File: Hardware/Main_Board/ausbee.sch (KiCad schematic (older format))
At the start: 0 parts

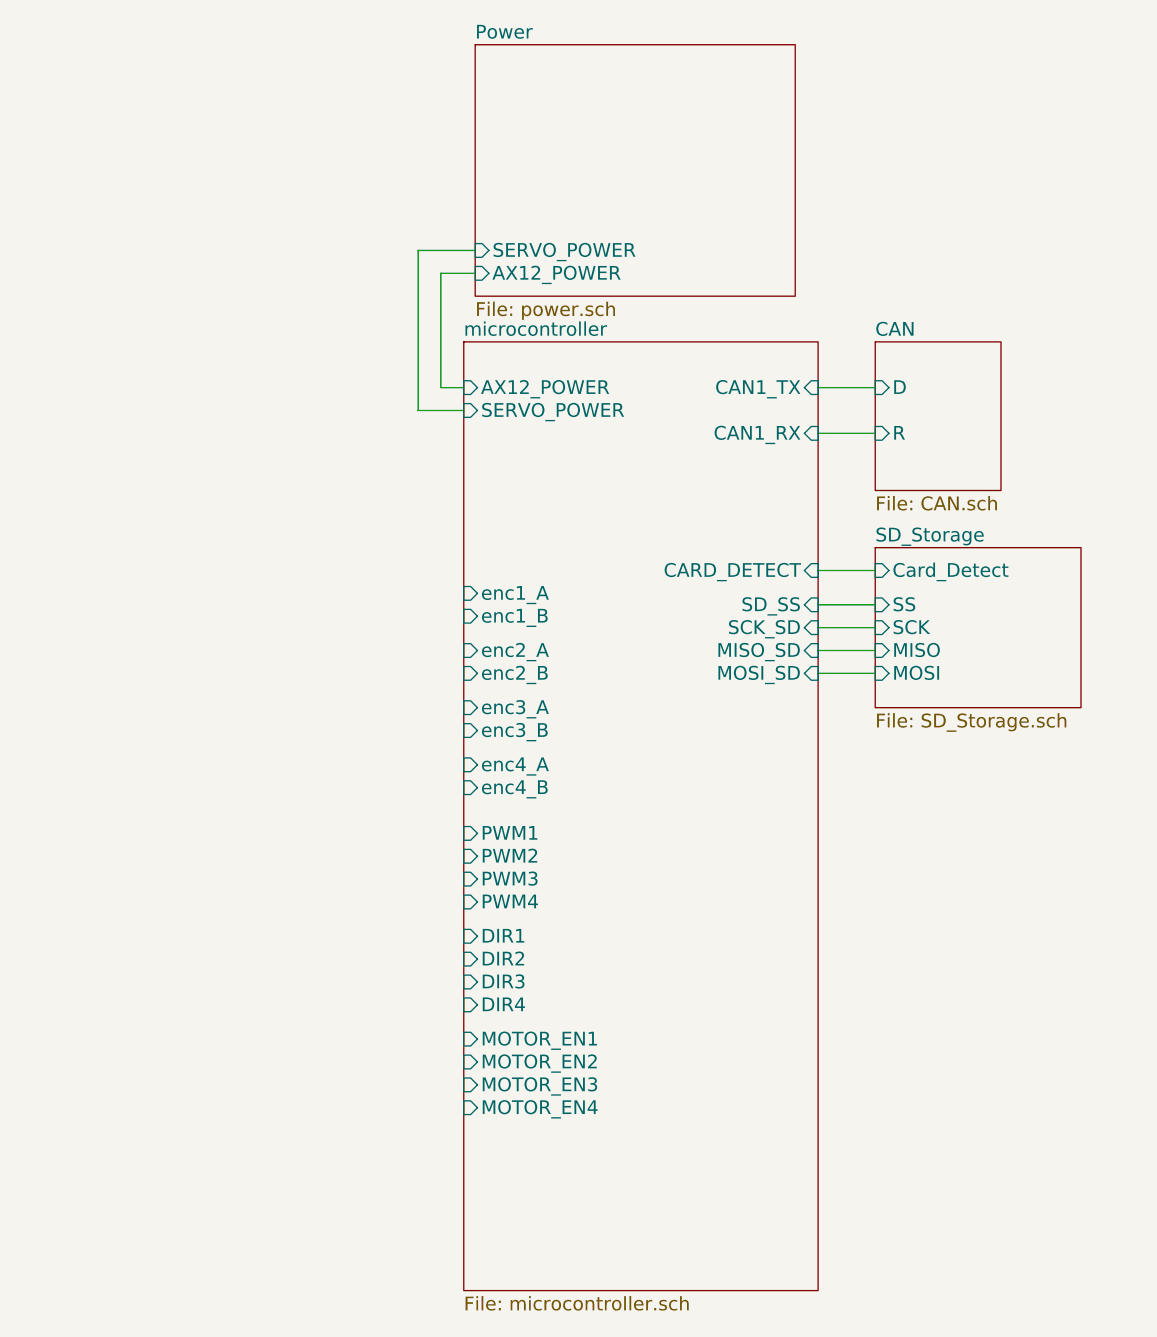
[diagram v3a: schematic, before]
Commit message: [HARDWARE] Finish motor interface and add SWD interface
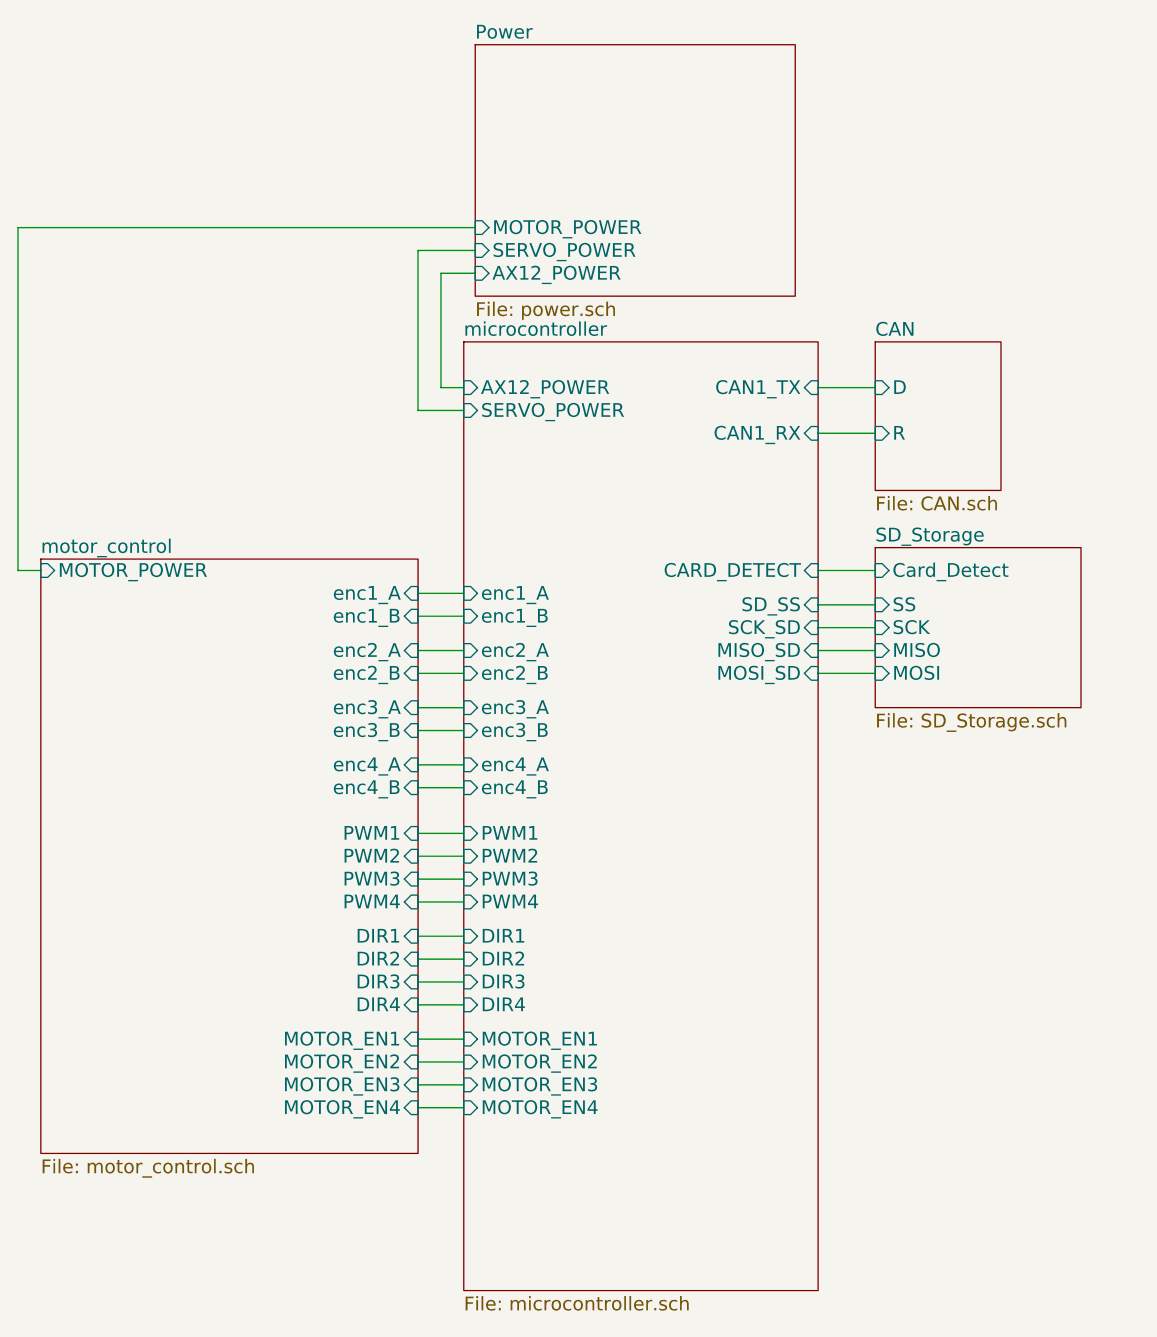
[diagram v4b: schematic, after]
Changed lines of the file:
@@
-EESchema Schematic File Version 2  date mer. 09 oct. 2013 08:53:10 CEST
+EESchema Schematic File Version 2  date mer. 09 oct. 2013 21:01:20 CEST
 LIBS:power
 LIBS:device
@@
 LIBS:sd_holder
 LIBS:ap1117
+LIBS:l298
 LIBS:ausbee-cache
 EELAYER 25  0
@@
 $Descr A4 11700 8267
 encoding utf-8
-Sheet 1 5
+Sheet 1 6
 Title ""
 Date "9 oct 2013"
@@
 $EndDescr
 Wire Wire Line
-	6050 3300 5800 3300
+	2400 3150 2300 3150
 Wire Wire Line
-	4250 2450 4050 2450
+	2300 3150 2300 1650
 Wire Wire Line
-	4050 2450 4050 1750
+	2300 1650 4300 1650
 Wire Wire Line
-	4050 1750 4300 1750
+	4050 5200 4250 5200
+Wire Wire Line
+	4250 4750 4050 4750
+Wire Wire Line
+	4050 4300 4250 4300
+Wire Wire Line
+	4050 5400 4250 5400
+Wire Wire Line
+	4050 4950 4250 4950
+Wire Wire Line
+	4050 4500 4250 4500
+Wire Wire Line
+	4050 4000 4250 4000
+Wire Wire Line
+	4050 3750 4250 3750
+Wire Wire Line
+	4050 3500 4250 3500
+Wire Wire Line
+	4050 3250 4250 3250
+Wire Wire Line
+	5800 3150 6050 3150
+Wire Wire Line
+	6050 3600 5800 3600
+Wire Wire Line
+	6050 3400 5800 3400
+Wire Wire Line
+	6050 2350 5800 2350
+Wire Wire Line
+	6050 2550 5800 2550
+Wire Wire Line
+	4300 1850 4150 1850
+Wire Wire Line
+	4150 1850 4150 2350
+Wire Wire Line
+	4150 2350 4250 2350
 Wire Wire Line
 	5800 3500 6050 3500
 Wire Wire Line
-	4250 2350 4150 2350
+	4300 1750 4050 1750
 Wire Wire Line
-	4150 2350 4150 1850
+	4050 1750 4050 2450
 Wire Wire Line
-	4150 1850 4300 1850
+	4050 2450 4250 2450
 Wire Wire Line
-	6050 2550 5800 2550
+	6050 3300 5800 3300
 Wire Wire Line
-	6050 2350 5800 2350
+	4250 3350 4050 3350
 Wire Wire Line
-	6050 3400 5800 3400
+	4250 3600 4050 3600
 Wire Wire Line
-	6050 3600 5800 3600
+	4250 3850 4050 3850
 Wire Wire Line
-	5800 3150 6050 3150
+	4250 4100 4050 4100
+Wire Wire Line
+	4250 4600 4050 4600
+Wire Wire Line
+	4250 5050 4050 5050
+Wire Wire Line
+	4250 5500 4050 5500
+Wire Wire Line
+	4250 4400 4050 4400
+Wire Wire Line
+	4250 4850 4050 4850
+Wire Wire Line
+	4250 5300 4050 5300
+$Sheet
+S 2400 3100 1650 2600
+U 5254FD6F
+F0 "motor_control" 60
+F1 "motor_control.sch" 60
+F2 "PWM4" I R 4050 4600 60
+F3 "DIR4" I R 4050 5050 60
+F4 "MOTOR_EN4" I R 4050 5500 60
+F5 "MOTOR_EN3" I R 4050 5400 60
+F6 "DIR3" I R 4050 4950 60
+F7 "PWM3" I R 4050 4500 60
+F8 "enc3_A" I R 4050 3750 60
+F9 "enc3_B" I R 4050 3850 60
+F10 "enc4_B" I R 4050 4100 60
+F11 "enc4_A" I R 4050 4000 60
+F12 "enc2_A" I R 4050 3500 60
+F13 "enc1_B" I R 4050 3350 60
+F14 "enc1_A" I R 4050 3250 60
+F15 "enc2_B" I R 4050 3600 60
+F16 "MOTOR_POWER" I L 2400 3150 60
+F17 "DIR1" I R 4050 4750 60
+F18 "DIR2" I R 4050 4850 60
+F19 "PWM1" I R 4050 4300 60
+F20 "PWM2" I R 4050 4400 60
+F21 "MOTOR_EN2" I R 4050 5300 60
+F22 "MOTOR_EN1" I R 4050 5200 60
+$EndSheet
 $Sheet
 S 4250 2150 1550 4150
@@
 F2 "AX12_POWER" I L 4300 1850 60
 F3 "SERVO_POWER" I L 4300 1750 60
+F4 "MOTOR_POWER" I L 4300 1650 60
 $EndSheet
 $Sheet

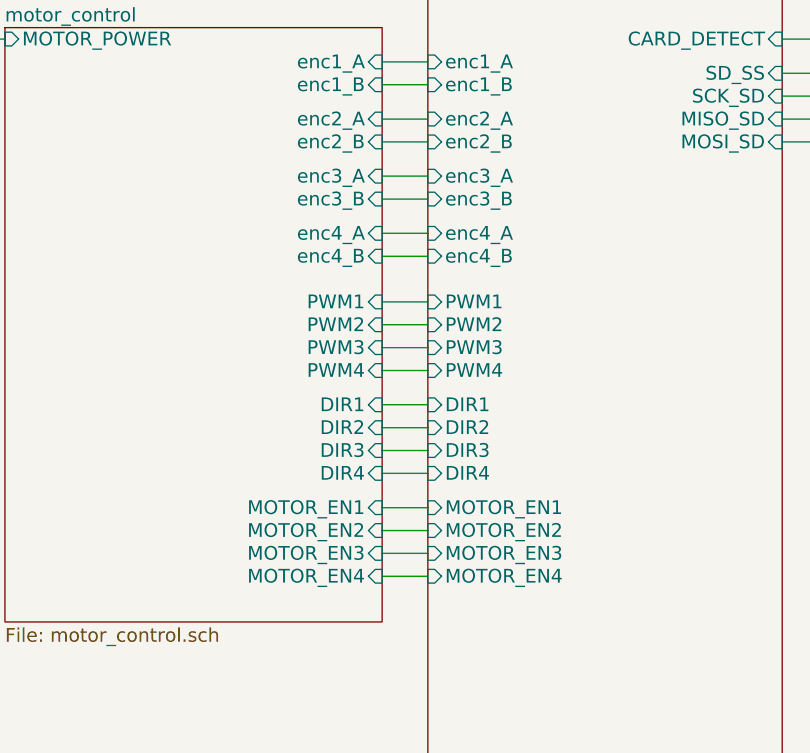
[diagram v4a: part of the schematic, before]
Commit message: [HARDWARE] Complete the SWD design, remove two undrived motor interfaces
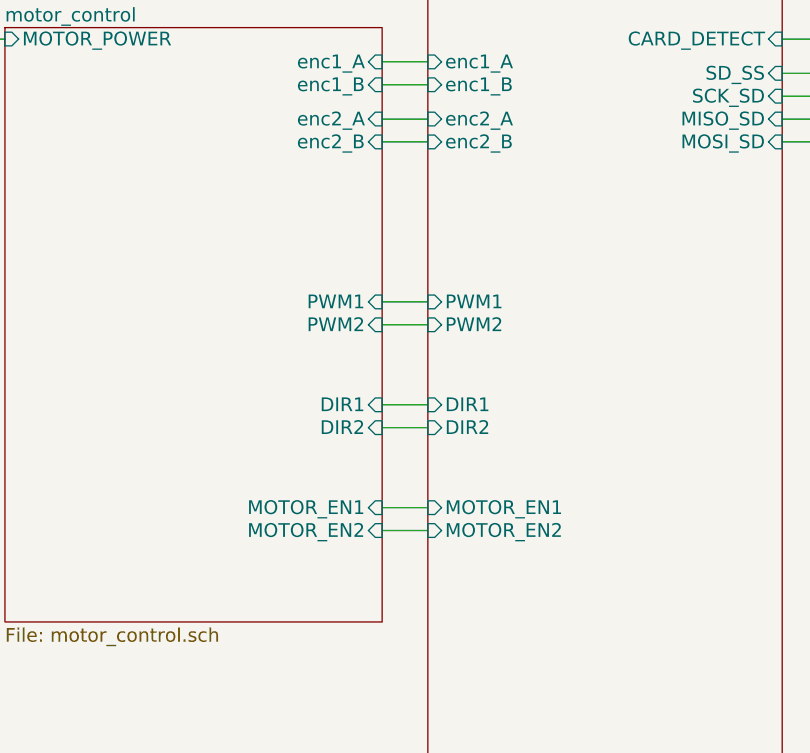
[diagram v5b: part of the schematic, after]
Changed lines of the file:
@@
-EESchema Schematic File Version 2  date mer. 09 oct. 2013 21:01:20 CEST
+EESchema Schematic File Version 2  date jeu. 10 oct. 2013 13:52:33 CEST
 LIBS:power
 LIBS:device
@@
 Sheet 1 6
 Title ""
-Date "9 oct 2013"
+Date "10 oct 2013"
 Rev ""
 Comp ""
@@
 Wire Wire Line
 	4050 4300 4250 4300
-Wire Wire Line
-	4050 5400 4250 5400
-Wire Wire Line
-	4050 4950 4250 4950
-Wire Wire Line
-	4050 4500 4250 4500
-Wire Wire Line
-	4050 4000 4250 4000
-Wire Wire Line
-	4050 3750 4250 3750
 Wire Wire Line
 	4050 3500 4250 3500
@@
 	4250 3600 4050 3600
 Wire Wire Line
-	4250 3850 4050 3850
-Wire Wire Line
-	4250 4100 4050 4100
-Wire Wire Line
-	4250 4600 4050 4600
-Wire Wire Line
-	4250 5050 4050 5050
-Wire Wire Line
-	4250 5500 4050 5500
-Wire Wire Line
 	4250 4400 4050 4400
 Wire Wire Line
@@
 F0 "motor_control" 60
 F1 "motor_control.sch" 60
-F2 "PWM4" I R 4050 4600 60
-F3 "DIR4" I R 4050 5050 60
-F4 "MOTOR_EN4" I R 4050 5500 60
-F5 "MOTOR_EN3" I R 4050 5400 60
-F6 "DIR3" I R 4050 4950 60
-F7 "PWM3" I R 4050 4500 60
-F8 "enc3_A" I R 4050 3750 60
-F9 "enc3_B" I R 4050 3850 60
-F10 "enc4_B" I R 4050 4100 60
-F11 "enc4_A" I R 4050 4000 60
-F12 "enc2_A" I R 4050 3500 60
-F13 "enc1_B" I R 4050 3350 60
-F14 "enc1_A" I R 4050 3250 60
-F15 "enc2_B" I R 4050 3600 60
-F16 "MOTOR_POWER" I L 2400 3150 60
-F17 "DIR1" I R 4050 4750 60
-F18 "DIR2" I R 4050 4850 60
-F19 "PWM1" I R 4050 4300 60
-F20 "PWM2" I R 4050 4400 60
-F21 "MOTOR_EN2" I R 4050 5300 60
-F22 "MOTOR_EN1" I R 4050 5200 60
+F8 "enc2_A" I R 4050 3500 60
+F9 "enc1_B" I R 4050 3350 60
+F10 "enc1_A" I R 4050 3250 60
+F11 "enc2_B" I R 4050 3600 60
+F12 "MOTOR_POWER" I L 2400 3150 60
+F13 "DIR1" I R 4050 4750 60
+F14 "DIR2" I R 4050 4850 60
+F15 "PWM1" I R 4050 4300 60
+F16 "PWM2" I R 4050 4400 60
+F17 "MOTOR_EN2" I R 4050 5300 60
+F18 "MOTOR_EN1" I R 4050 5200 60
 $EndSheet
 $Sheet
@@
 F2 "CAN1_TX" I R 5800 2350 60
 F3 "CAN1_RX" I R 5800 2550 60
-F4 "enc4_B" I L 4250 4100 60
-F5 "enc4_A" I L 4250 4000 60
-F6 "enc3_B" I L 4250 3850 60
-F7 "enc3_A" I L 4250 3750 60
 F8 "enc2_B" I L 4250 3600 60
 F9 "enc2_A" I L 4250 3500 60
 F10 "enc1_B" I L 4250 3350 60
 F11 "enc1_A" I L 4250 3250 60
-F12 "PWM4" I L 4250 4600 60
-F13 "PWM3" I L 4250 4500 60
 F14 "PWM2" I L 4250 4400 60
 F15 "PWM1" I L 4250 4300 60
@@
 F19 "MISO_SD" I R 5800 3500 60
 F20 "SERVO_POWER" I L 4250 2450 60
-F21 "MOTOR_EN4" I L 4250 5500 60
-F22 "MOTOR_EN3" I L 4250 5400 60
-F23 "DIR4" I L 4250 5050 60
-F24 "DIR3" I L 4250 4950 60
 F25 "MOTOR_EN2" I L 4250 5300 60
 F26 "MOTOR_EN1" I L 4250 5200 60
